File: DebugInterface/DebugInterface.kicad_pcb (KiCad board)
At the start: 2 copper layers, 157 x 169.9 mm, 38 parts, among them J1 IDC-50M, J10 Barrel_Jack_MountingPin, J11 ISP, J2 IDC-50M, J3 IDC-50M, J4 IDC-50M, J5 IDC-50M, J6 IDC-50M, J7 IDC-50M, J8 IDC-50M, J9 USB_B, U1 8255, U10 PIC18F2550-ISO, U2 8255, U3 8255, U4 8255, U5 8255, U6 8255, U7 8255, U8 8255, U9 74LS138, Y1 20MHz

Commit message: DebugInterface: Some layout touchups
Better copper fill
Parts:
- moved C8 1.50 mm to (148.8, 84.1)
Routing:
- net GND: track 1661.3 -> 1660.5 mm

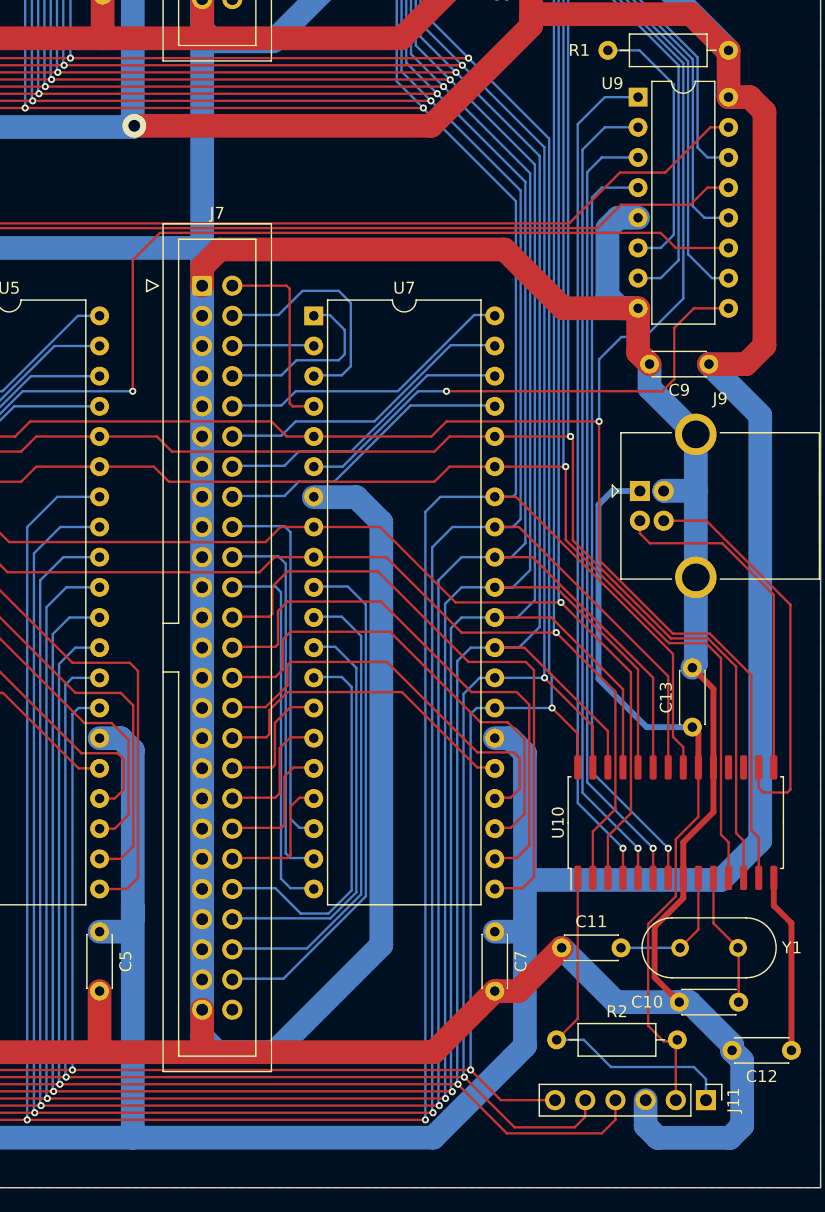
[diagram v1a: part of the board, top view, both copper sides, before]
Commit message: DebugInterface: Fix ISP connector
Proper pin assignment
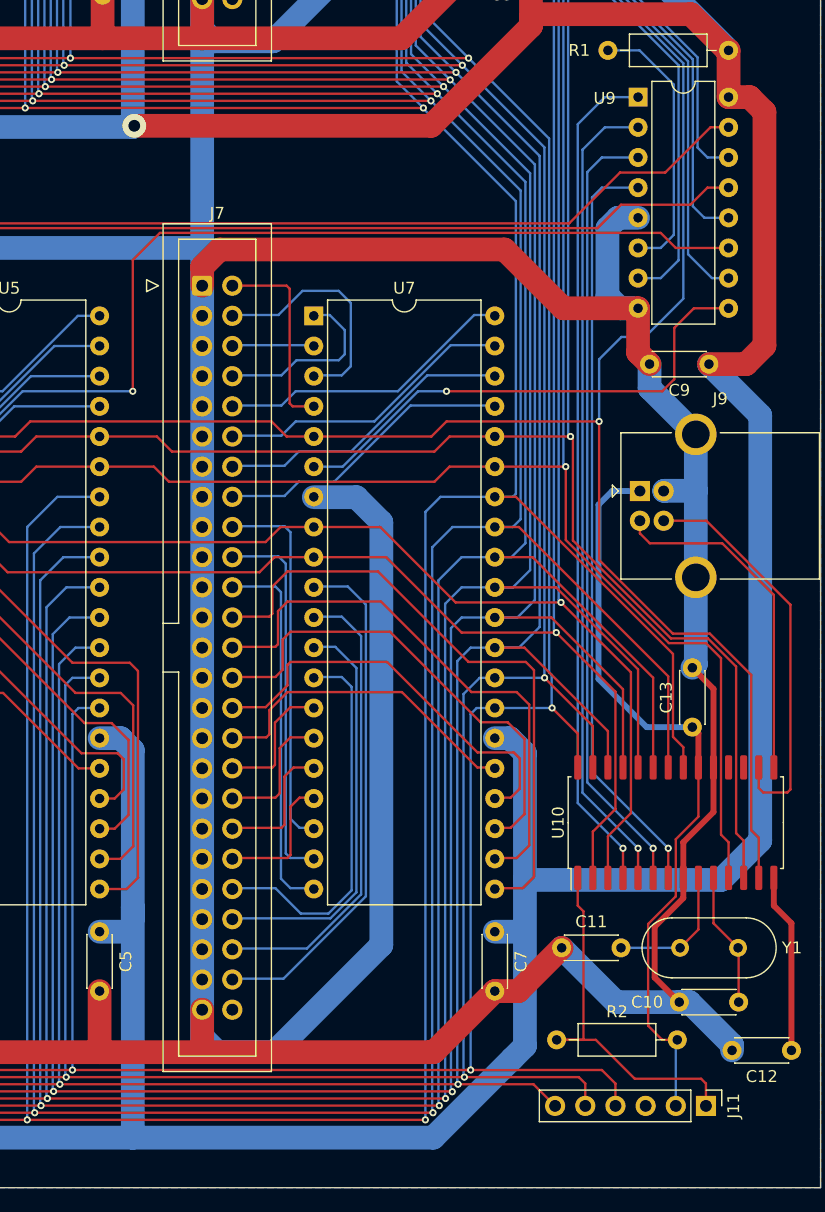
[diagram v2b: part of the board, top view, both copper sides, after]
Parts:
- moved J11 0.48 mm to (163.6, 179.8)
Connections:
- J11 pad 4: /D5 -> /D7
- J11 pad 6: /D7 -> /D5
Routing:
- net GND: track 1660.5 -> 1642.7 mm
- net /D5: track 600.2 -> 592.1 mm
- net /D7: track 535.6 -> 542.4 mm
- net Net-(J11-Pin_1): track 30.1 -> 32.1 mm
- net /D6: track 566.9 -> 565.5 mm

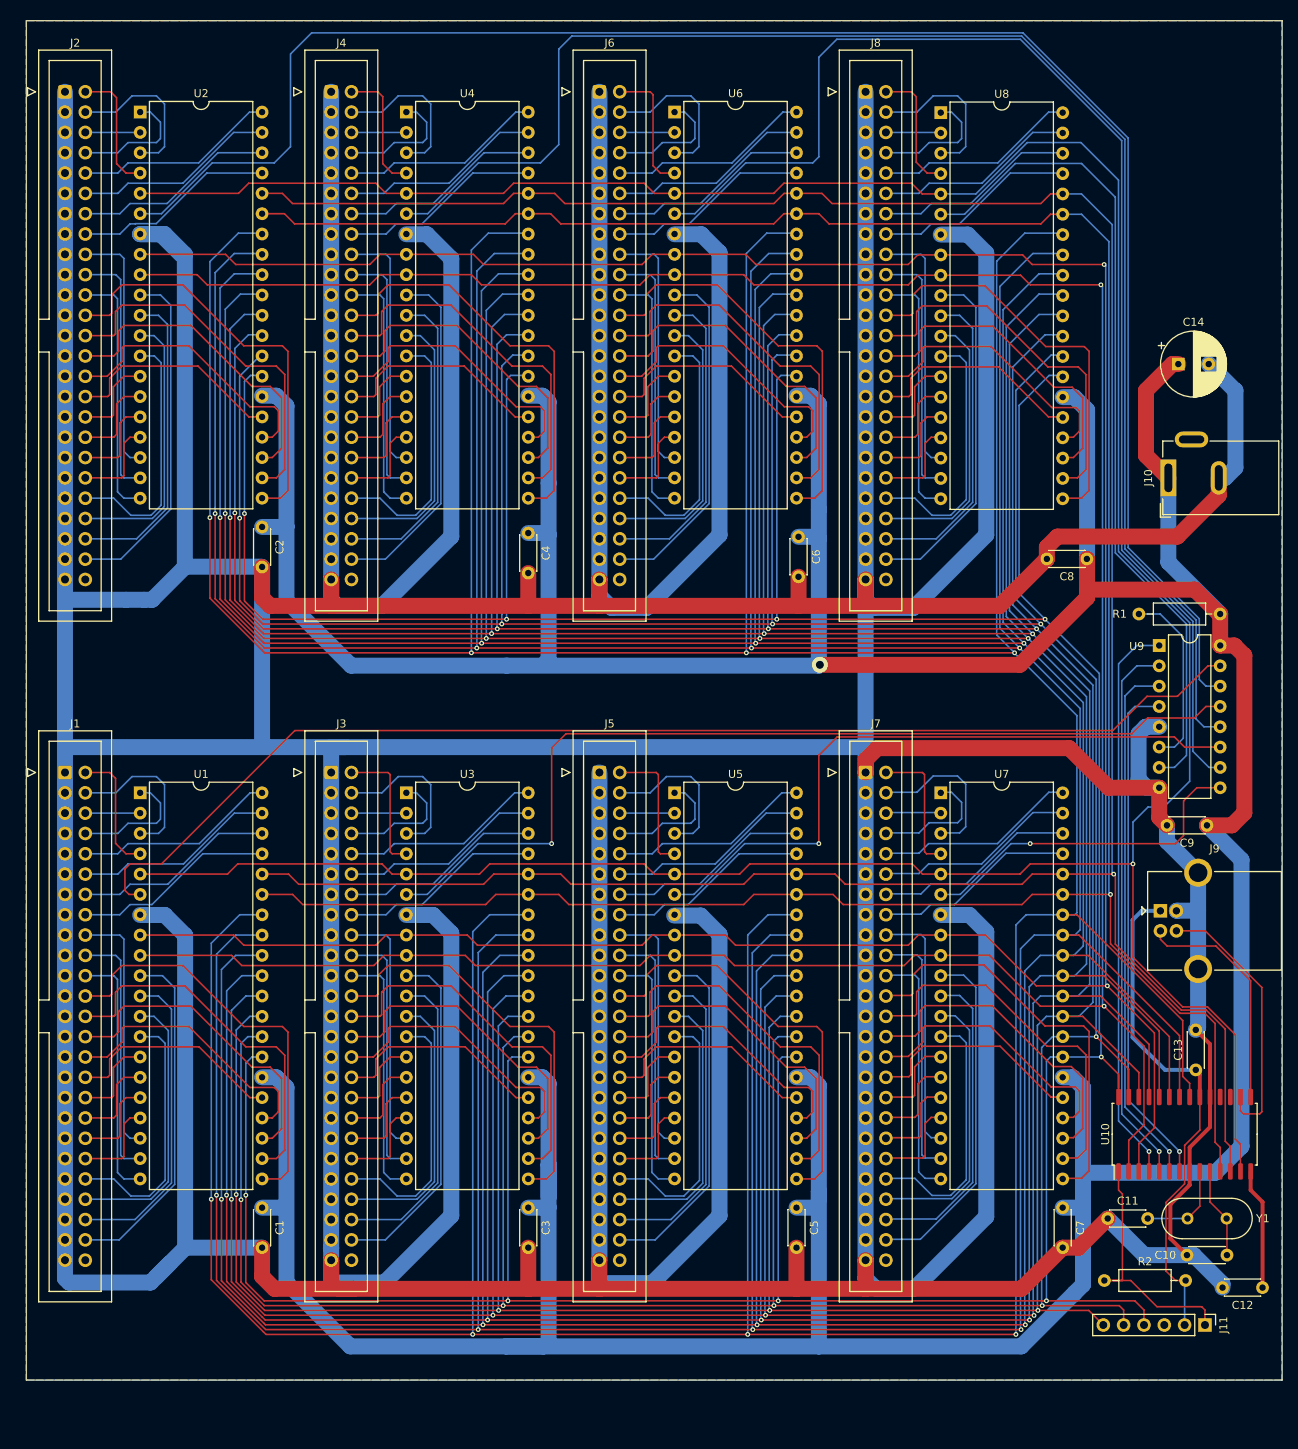
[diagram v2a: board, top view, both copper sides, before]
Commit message: DebugInterface: Second version
Each port has got own connector for ease of separation and making cables.
Ports are rearranged in address space to enable longer sequential
reads/writes
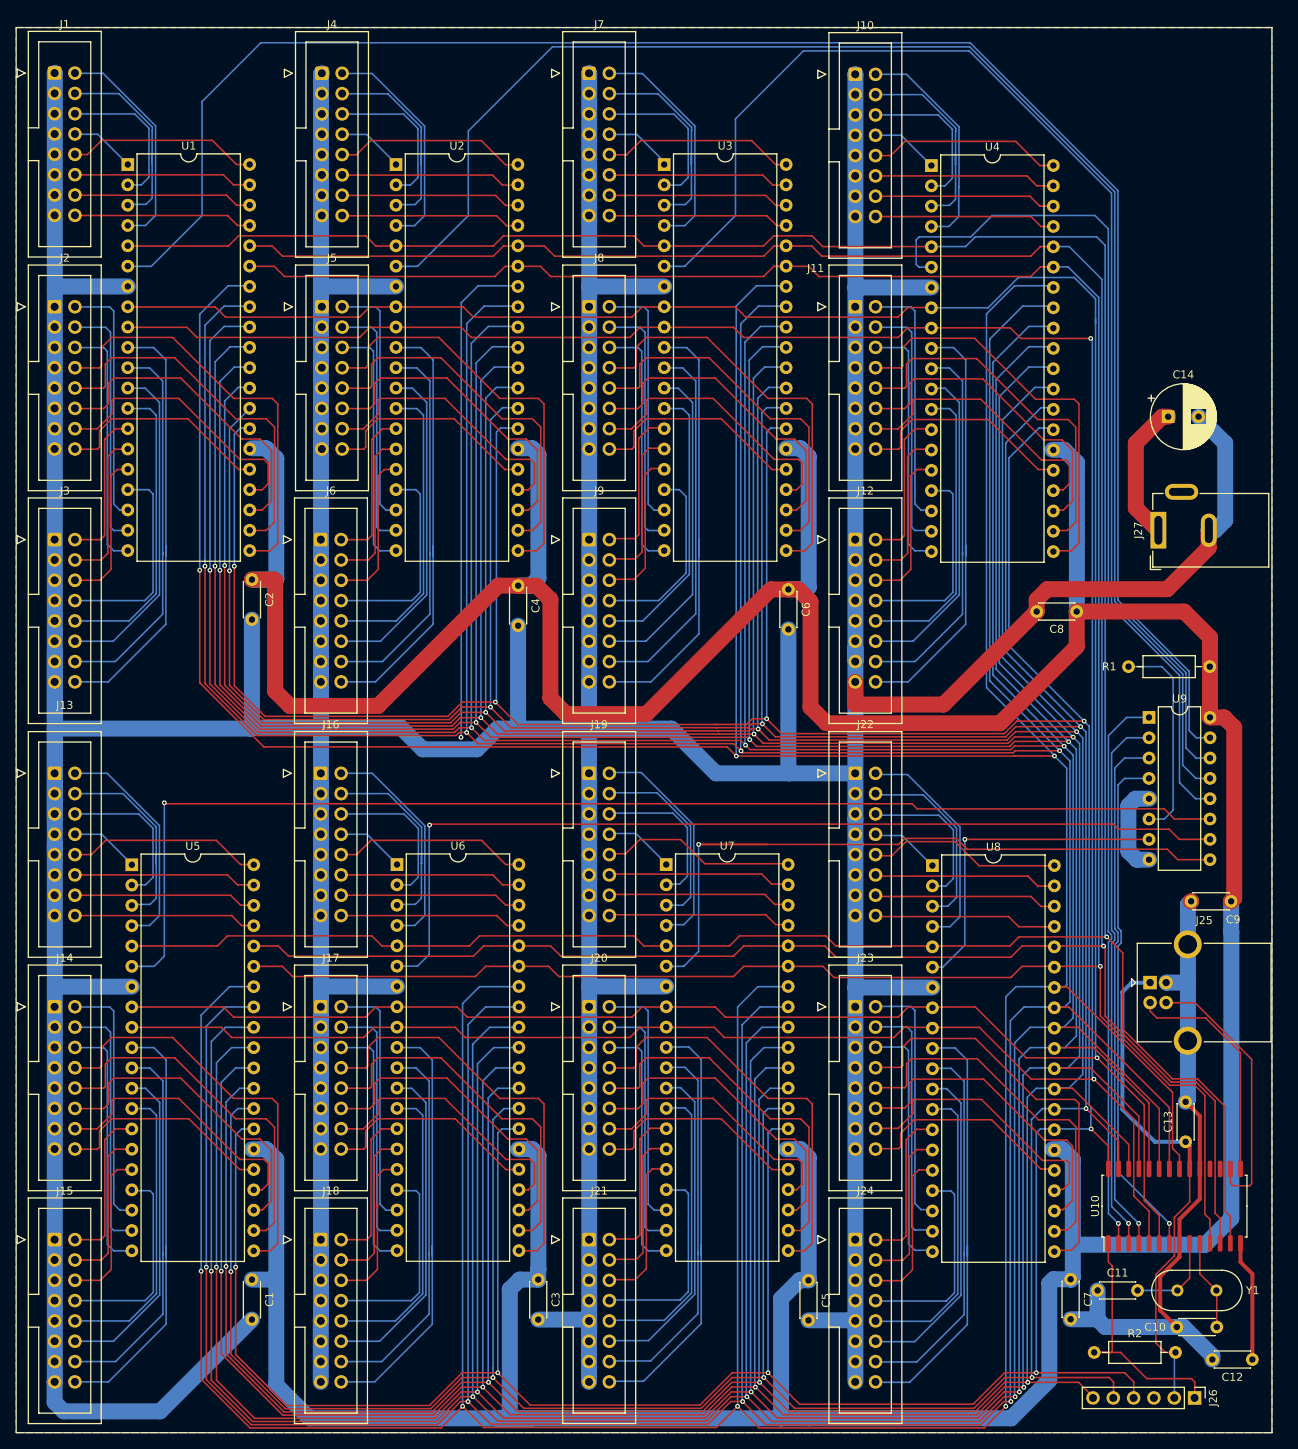
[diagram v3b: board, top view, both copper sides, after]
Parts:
- added J12: IDC-16M, Connector_IDC:IDC-Header_2x08_P2.54mm_Vertical, F.Cu at (119.9, 81.7)
- added J13: IDC-16M, Connector_IDC:IDC-Header_2x08_P2.54mm_Vertical, F.Cu at (19.8, 110.9)
- added J14: IDC-16M, Connector_IDC:IDC-Header_2x08_P2.54mm_Vertical, F.Cu at (19.8, 140.1)
- added J15: IDC-16M, Connector_IDC:IDC-Header_2x08_P2.54mm_Vertical, F.Cu at (19.8, 169.2)
- added J16: IDC-16M, Connector_IDC:IDC-Header_2x08_P2.54mm_Vertical, F.Cu at (53.1, 110.9)
- added J17: IDC-16M, Connector_IDC:IDC-Header_2x08_P2.54mm_Vertical, F.Cu at (53.1, 140.1)
- added J18: IDC-16M, Connector_IDC:IDC-Header_2x08_P2.54mm_Vertical, F.Cu at (53.1, 169.2)
- added J19: IDC-16M, Connector_IDC:IDC-Header_2x08_P2.54mm_Vertical, F.Cu at (86.6, 110.9)
- added J20: IDC-16M, Connector_IDC:IDC-Header_2x08_P2.54mm_Vertical, F.Cu at (86.6, 140.1)
- added J21: IDC-16M, Connector_IDC:IDC-Header_2x08_P2.54mm_Vertical, F.Cu at (86.6, 169.2)
- added J22: IDC-16M, Connector_IDC:IDC-Header_2x08_P2.54mm_Vertical, F.Cu at (119.9, 110.9)
- added J23: IDC-16M, Connector_IDC:IDC-Header_2x08_P2.54mm_Vertical, F.Cu at (119.9, 140.1)
- added J24: IDC-16M, Connector_IDC:IDC-Header_2x08_P2.54mm_Vertical, F.Cu at (119.9, 169.2)
- added J25: USB_B, Connector_USB:USB_B_OST_USB-B1HSxx_Horizontal, F.Cu at (156.7, 137.0)
- added J26: ISP, Connector_PinHeader_2.54mm:PinHeader_1x06_P2.54mm_Vertical, F.Cu at (162.3, 188.9)
- added J27: Barrel_Jack_MountingPin, Connector_BarrelJack:BarrelJack_GCT_DCJ200-10-A_Horizontal, F.Cu at (157.8, 80.5)
- J1, J2, J3, J4, J5, J6, J7, J8: value IDC-50M -> IDC-16M; footprint Connector_IDC:IDC-Header_2x25_P2.54mm_Vertical -> Connector_IDC:IDC-Header_2x08_P2.54mm_Vertical
- J10: value Barrel_Jack_MountingPin -> IDC-16M; footprint Connector_BarrelJack:BarrelJack_GCT_DCJ200-10-A_Horizontal -> Connector_IDC:IDC-Header_2x08_P2.54mm_Vertical
- J11: value ISP -> IDC-16M; footprint Connector_PinHeader_2.54mm:PinHeader_1x06_P2.54mm_Vertical -> Connector_IDC:IDC-Header_2x08_P2.54mm_Vertical
- J9: value USB_B -> IDC-16M; footprint Connector_USB:USB_B_OST_USB-B1HSxx_Horizontal -> Connector_IDC:IDC-Header_2x08_P2.54mm_Vertical
- moved J11 134.6 mm to (119.9, 52.6), turned to 0 degrees
- moved U6 100.3 mm to (62.6, 122.3)
- moved U8 94.1 mm to (129.5, 122.4)
- moved J7 94.0 mm to (86.6, 23.4)
- moved J1 87.4 mm to (19.8, 23.3)
- moved J9 85.2 mm to (86.6, 81.7)
- moved U3 84.9 mm to (96.0, 34.8)
- moved U1 78.6 mm to (29.0, 34.8)
- moved U5 68.4 mm to (29.5, 122.3)
- moved J5 67.8 mm to (53.2, 52.6)
- moved U4 66.0 mm to (129.4, 34.9)
- moved J6 65.9 mm to (53.1, 81.7)
- moved J10 63.8 mm to (119.9, 23.5), turned to 0 degrees
- moved J3 45.2 mm to (19.8, 81.7)
- moved J8 43.8 mm to (86.6, 52.6)
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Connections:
- C13 pad 1: Net-(J11-Pin_2) -> Net-(J25-VBUS)
- J10 pad 1: VCC -> GND
- J10 pad 2: GND -> Net-(J10-Pin_2)
- J10 pad 3: (no net) -> GND
- J11 pad 1: Net-(J11-Pin_1) -> GND
- J11 pad 4: /D7 -> Net-(J11-Pin_4)
- J11 pad 5: /D6 -> GND
- J11 pad 6: /D5 -> Net-(J11-Pin_6)
- J9 pad 1: Net-(J11-Pin_2) -> GND
- J9 pad 2: Net-(J9-D-) -> Net-(J9-Pin_2)
- J9 pad 3: Net-(J9-D+) -> GND
- J9 pad 4: GND -> Net-(J9-Pin_4)
- R2 pad 1: Net-(J11-Pin_1) -> Net-(J26-Pin_1)
- R2 pad 2: Net-(J11-Pin_2) -> Net-(J25-VBUS)
- U1 pad 10: Net-(J1-Pin_48) -> Net-(J3-Pin_16)
- U1 pad 11: Net-(J1-Pin_46) -> Net-(J3-Pin_14)
- U1 pad 12: Net-(J1-Pin_44) -> Net-(J3-Pin_12)
- U1 pad 13: Net-(J1-Pin_42) -> Net-(J3-Pin_10)
- U1 pad 14: Net-(J1-Pin_34) -> Net-(J3-Pin_2)
- U1 pad 15: Net-(J1-Pin_36) -> Net-(J3-Pin_4)
- U1 pad 16: Net-(J1-Pin_38) -> Net-(J3-Pin_6)
- U1 pad 17: Net-(J1-Pin_40) -> Net-(J3-Pin_8)
- U1 pad 18: Net-(J1-Pin_18) -> Net-(J2-Pin_2)
- U1 pad 19: Net-(J1-Pin_20) -> Net-(J2-Pin_4)
- U1 pad 20: Net-(J1-Pin_22) -> Net-(J2-Pin_6)
- U1 pad 21: Net-(J1-Pin_24) -> Net-(J2-Pin_8)
- U1 pad 22: Net-(J1-Pin_26) -> Net-(J2-Pin_10)
- U1 pad 23: Net-(J1-Pin_28) -> Net-(J2-Pin_12)
- U1 pad 24: Net-(J1-Pin_30) -> Net-(J2-Pin_14)
- U1 pad 25: Net-(J1-Pin_32) -> Net-(J2-Pin_16)
- U1 pad 8: /A1 -> /A4
- U1 pad 9: /A0 -> /A3
- U10 pad 1: Net-(J11-Pin_1) -> Net-(J26-Pin_1)
- U10 pad 15: Net-(J9-D-) -> Net-(J25-D-)
- U10 pad 16: Net-(J9-D+) -> Net-(J25-D+)
- U10 pad 20: Net-(J11-Pin_2) -> Net-(J25-VBUS)
- U2 pad 1: Net-(J2-Pin_8) -> Net-(J4-Pin_8)
- U2 pad 10: Net-(J2-Pin_48) -> Net-(J6-Pin_16)
- U2 pad 11: Net-(J2-Pin_46) -> Net-(J6-Pin_14)
- U2 pad 12: Net-(J2-Pin_44) -> Net-(J6-Pin_12)
- U2 pad 13: Net-(J2-Pin_42) -> Net-(J6-Pin_10)
- U2 pad 14: Net-(J2-Pin_34) -> Net-(J6-Pin_2)
- U2 pad 15: Net-(J2-Pin_36) -> Net-(J6-Pin_4)
- U2 pad 16: Net-(J2-Pin_38) -> Net-(J6-Pin_6)
- U2 pad 17: Net-(J2-Pin_40) -> Net-(J6-Pin_8)
- U2 pad 18: Net-(J2-Pin_18) -> Net-(J5-Pin_2)
- U2 pad 19: Net-(J2-Pin_20) -> Net-(J5-Pin_4)
- U2 pad 2: Net-(J2-Pin_6) -> Net-(J4-Pin_6)
- U2 pad 20: Net-(J2-Pin_22) -> Net-(J5-Pin_6)
- U2 pad 21: Net-(J2-Pin_24) -> Net-(J5-Pin_8)
- U2 pad 22: Net-(J2-Pin_26) -> Net-(J5-Pin_10)
- U2 pad 23: Net-(J2-Pin_28) -> Net-(J5-Pin_12)
- U2 pad 24: Net-(J2-Pin_30) -> Net-(J5-Pin_14)
- U2 pad 25: Net-(J2-Pin_32) -> Net-(J5-Pin_16)
- U2 pad 3: Net-(J2-Pin_4) -> Net-(J4-Pin_4)
- U2 pad 37: Net-(J2-Pin_16) -> Net-(J4-Pin_16)
- U2 pad 38: Net-(J2-Pin_14) -> Net-(J4-Pin_14)
- U2 pad 39: Net-(J2-Pin_12) -> Net-(J4-Pin_12)
- U2 pad 4: Net-(J2-Pin_2) -> Net-(J4-Pin_2)
- U2 pad 40: Net-(J2-Pin_10) -> Net-(J4-Pin_10)
- U2 pad 8: /A1 -> /A4
- U2 pad 9: /A0 -> /A3
- U3 pad 1: Net-(J3-Pin_8) -> Net-(J7-Pin_8)
- U3 pad 10: Net-(J3-Pin_48) -> Net-(J9-Pin_16)
- U3 pad 11: Net-(J3-Pin_46) -> Net-(J9-Pin_14)
- U3 pad 12: Net-(J3-Pin_44) -> Net-(J9-Pin_12)
- U3 pad 13: Net-(J3-Pin_42) -> Net-(J9-Pin_10)
- U3 pad 14: Net-(J3-Pin_34) -> Net-(J9-Pin_2)
- U3 pad 15: Net-(J3-Pin_36) -> Net-(J9-Pin_4)
- U3 pad 16: Net-(J3-Pin_38) -> Net-(J9-Pin_6)
- U3 pad 17: Net-(J3-Pin_40) -> Net-(J9-Pin_8)
- U3 pad 18: Net-(J3-Pin_18) -> Net-(J8-Pin_2)
- U3 pad 19: Net-(J3-Pin_20) -> Net-(J8-Pin_4)
- U3 pad 2: Net-(J3-Pin_6) -> Net-(J7-Pin_6)
- U3 pad 20: Net-(J3-Pin_22) -> Net-(J8-Pin_6)
- U3 pad 21: Net-(J3-Pin_24) -> Net-(J8-Pin_8)
- U3 pad 22: Net-(J3-Pin_26) -> Net-(J8-Pin_10)
- U3 pad 23: Net-(J3-Pin_28) -> Net-(J8-Pin_12)
- U3 pad 24: Net-(J3-Pin_30) -> Net-(J8-Pin_14)
- U3 pad 25: Net-(J3-Pin_32) -> Net-(J8-Pin_16)
- U3 pad 3: Net-(J3-Pin_4) -> Net-(J7-Pin_4)
- U3 pad 37: Net-(J3-Pin_16) -> Net-(J7-Pin_16)
- U3 pad 38: Net-(J3-Pin_14) -> Net-(J7-Pin_14)
- U3 pad 39: Net-(J3-Pin_12) -> Net-(J7-Pin_12)
- U3 pad 4: Net-(J3-Pin_2) -> Net-(J7-Pin_2)
- U3 pad 40: Net-(J3-Pin_10) -> Net-(J7-Pin_10)
- U3 pad 8: /A1 -> /A4
- U3 pad 9: /A0 -> /A3
- U4 pad 1: Net-(J4-Pin_8) -> Net-(J10-Pin_8)
- U4 pad 10: Net-(J4-Pin_48) -> Net-(J12-Pin_16)
- U4 pad 11: Net-(J4-Pin_46) -> Net-(J12-Pin_14)
- U4 pad 12: Net-(J4-Pin_44) -> Net-(J12-Pin_12)
- U4 pad 13: Net-(J4-Pin_42) -> Net-(J12-Pin_10)
- U4 pad 14: Net-(J4-Pin_34) -> Net-(J12-Pin_2)
- U4 pad 15: Net-(J4-Pin_36) -> Net-(J12-Pin_4)
- U4 pad 16: Net-(J4-Pin_38) -> Net-(J12-Pin_6)
- U4 pad 17: Net-(J4-Pin_40) -> Net-(J12-Pin_8)
- U4 pad 18: Net-(J4-Pin_18) -> Net-(J11-Pin_2)
- U4 pad 19: Net-(J4-Pin_20) -> Net-(J11-Pin_4)
- U4 pad 2: Net-(J4-Pin_6) -> Net-(J10-Pin_6)
- U4 pad 20: Net-(J4-Pin_22) -> Net-(J11-Pin_6)
- U4 pad 21: Net-(J4-Pin_24) -> Net-(J11-Pin_8)
- U4 pad 22: Net-(J4-Pin_26) -> Net-(J11-Pin_10)
- U4 pad 23: Net-(J4-Pin_28) -> Net-(J11-Pin_12)
- U4 pad 24: Net-(J4-Pin_30) -> Net-(J11-Pin_14)
- U4 pad 25: Net-(J4-Pin_32) -> Net-(J11-Pin_16)
- U4 pad 3: Net-(J4-Pin_4) -> Net-(J10-Pin_4)
- U4 pad 37: Net-(J4-Pin_16) -> Net-(J10-Pin_16)
- U4 pad 38: Net-(J4-Pin_14) -> Net-(J10-Pin_14)
- U4 pad 39: Net-(J4-Pin_12) -> Net-(J10-Pin_12)
- U4 pad 4: Net-(J4-Pin_2) -> Net-(J10-Pin_2)
- U4 pad 40: Net-(J4-Pin_10) -> Net-(J10-Pin_10)
- U4 pad 8: /A1 -> /A4
- U4 pad 9: /A0 -> /A3
- U5 pad 1: Net-(J5-Pin_8) -> Net-(J13-Pin_8)
- U5 pad 10: Net-(J5-Pin_48) -> Net-(J15-Pin_16)
- U5 pad 11: Net-(J5-Pin_46) -> Net-(J15-Pin_14)
- U5 pad 12: Net-(J5-Pin_44) -> Net-(J15-Pin_12)
- U5 pad 13: Net-(J5-Pin_42) -> Net-(J15-Pin_10)
- U5 pad 14: Net-(J5-Pin_34) -> Net-(J15-Pin_2)
- U5 pad 15: Net-(J5-Pin_36) -> Net-(J15-Pin_4)
- U5 pad 16: Net-(J5-Pin_38) -> Net-(J15-Pin_6)
- U5 pad 17: Net-(J5-Pin_40) -> Net-(J15-Pin_8)
- U5 pad 18: Net-(J5-Pin_18) -> Net-(J14-Pin_2)
- U5 pad 19: Net-(J5-Pin_20) -> Net-(J14-Pin_4)
- U5 pad 2: Net-(J5-Pin_6) -> Net-(J13-Pin_6)
- U5 pad 20: Net-(J5-Pin_22) -> Net-(J14-Pin_6)
- U5 pad 21: Net-(J5-Pin_24) -> Net-(J14-Pin_8)
- U5 pad 22: Net-(J5-Pin_26) -> Net-(J14-Pin_10)
- U5 pad 23: Net-(J5-Pin_28) -> Net-(J14-Pin_12)
- U5 pad 24: Net-(J5-Pin_30) -> Net-(J14-Pin_14)
- U5 pad 25: Net-(J5-Pin_32) -> Net-(J14-Pin_16)
- U5 pad 3: Net-(J5-Pin_4) -> Net-(J13-Pin_4)
- U5 pad 37: Net-(J5-Pin_16) -> Net-(J13-Pin_16)
- U5 pad 38: Net-(J5-Pin_14) -> Net-(J13-Pin_14)
- U5 pad 39: Net-(J5-Pin_12) -> Net-(J13-Pin_12)
- U5 pad 4: Net-(J5-Pin_2) -> Net-(J13-Pin_2)
- U5 pad 40: Net-(J5-Pin_10) -> Net-(J13-Pin_10)
- U5 pad 8: /A1 -> /A4
- U5 pad 9: /A0 -> /A3
- U6 pad 1: Net-(J6-Pin_8) -> Net-(J16-Pin_8)
- U6 pad 10: Net-(J6-Pin_48) -> Net-(J18-Pin_16)
- U6 pad 11: Net-(J6-Pin_46) -> Net-(J18-Pin_14)
- U6 pad 12: Net-(J6-Pin_44) -> Net-(J18-Pin_12)
- U6 pad 13: Net-(J6-Pin_42) -> Net-(J18-Pin_10)
- U6 pad 14: Net-(J6-Pin_34) -> Net-(J18-Pin_2)
- U6 pad 15: Net-(J6-Pin_36) -> Net-(J18-Pin_4)
- U6 pad 16: Net-(J6-Pin_38) -> Net-(J18-Pin_6)
- U6 pad 17: Net-(J6-Pin_40) -> Net-(J18-Pin_8)
- U6 pad 18: Net-(J6-Pin_18) -> Net-(J17-Pin_2)
- U6 pad 19: Net-(J6-Pin_20) -> Net-(J17-Pin_4)
- U6 pad 2: Net-(J6-Pin_6) -> Net-(J16-Pin_6)
- U6 pad 20: Net-(J6-Pin_22) -> Net-(J17-Pin_6)
- U6 pad 21: Net-(J6-Pin_24) -> Net-(J17-Pin_8)
- U6 pad 22: Net-(J6-Pin_26) -> Net-(J17-Pin_10)
- U6 pad 23: Net-(J6-Pin_28) -> Net-(J17-Pin_12)
- U6 pad 24: Net-(J6-Pin_30) -> Net-(J17-Pin_14)
- U6 pad 25: Net-(J6-Pin_32) -> Net-(J17-Pin_16)
- U6 pad 3: Net-(J6-Pin_4) -> Net-(J16-Pin_4)
- U6 pad 37: Net-(J6-Pin_16) -> Net-(J16-Pin_16)
- U6 pad 38: Net-(J6-Pin_14) -> Net-(J16-Pin_14)
- U6 pad 39: Net-(J6-Pin_12) -> Net-(J16-Pin_12)
- U6 pad 4: Net-(J6-Pin_2) -> Net-(J16-Pin_2)
- U6 pad 40: Net-(J6-Pin_10) -> Net-(J16-Pin_10)
- U6 pad 8: /A1 -> /A4
- U6 pad 9: /A0 -> /A3
- U7 pad 1: Net-(J7-Pin_8) -> Net-(J19-Pin_8)
- U7 pad 10: Net-(J7-Pin_48) -> Net-(J21-Pin_16)
- U7 pad 11: Net-(J7-Pin_46) -> Net-(J21-Pin_14)
- U7 pad 12: Net-(J7-Pin_44) -> Net-(J21-Pin_12)
- U7 pad 13: Net-(J7-Pin_42) -> Net-(J21-Pin_10)
- U7 pad 14: Net-(J7-Pin_34) -> Net-(J21-Pin_2)
- U7 pad 15: Net-(J7-Pin_36) -> Net-(J21-Pin_4)
- U7 pad 16: Net-(J7-Pin_38) -> Net-(J21-Pin_6)
- U7 pad 17: Net-(J7-Pin_40) -> Net-(J21-Pin_8)
- U7 pad 18: Net-(J7-Pin_18) -> Net-(J20-Pin_2)
- U7 pad 19: Net-(J7-Pin_20) -> Net-(J20-Pin_4)
- U7 pad 2: Net-(J7-Pin_6) -> Net-(J19-Pin_6)
- U7 pad 20: Net-(J7-Pin_22) -> Net-(J20-Pin_6)
- U7 pad 21: Net-(J7-Pin_24) -> Net-(J20-Pin_8)
- U7 pad 22: Net-(J7-Pin_26) -> Net-(J20-Pin_10)
- U7 pad 23: Net-(J7-Pin_28) -> Net-(J20-Pin_12)
- U7 pad 24: Net-(J7-Pin_30) -> Net-(J20-Pin_14)
- U7 pad 25: Net-(J7-Pin_32) -> Net-(J20-Pin_16)
- U7 pad 3: Net-(J7-Pin_4) -> Net-(J19-Pin_4)
- U7 pad 37: Net-(J7-Pin_16) -> Net-(J19-Pin_16)
- U7 pad 38: Net-(J7-Pin_14) -> Net-(J19-Pin_14)
- U7 pad 39: Net-(J7-Pin_12) -> Net-(J19-Pin_12)
- U7 pad 4: Net-(J7-Pin_2) -> Net-(J19-Pin_2)
- U7 pad 40: Net-(J7-Pin_10) -> Net-(J19-Pin_10)
- U7 pad 8: /A1 -> /A4
- U7 pad 9: /A0 -> /A3
- U8 pad 1: Net-(J8-Pin_8) -> Net-(J22-Pin_8)
- U8 pad 10: Net-(J8-Pin_48) -> Net-(J24-Pin_16)
- U8 pad 11: Net-(J8-Pin_46) -> Net-(J24-Pin_14)
- U8 pad 12: Net-(J8-Pin_44) -> Net-(J24-Pin_12)
- U8 pad 13: Net-(J8-Pin_42) -> Net-(J24-Pin_10)
- U8 pad 14: Net-(J8-Pin_34) -> Net-(J24-Pin_2)
- U8 pad 15: Net-(J8-Pin_36) -> Net-(J24-Pin_4)
- U8 pad 16: Net-(J8-Pin_38) -> Net-(J24-Pin_6)
- U8 pad 17: Net-(J8-Pin_40) -> Net-(J24-Pin_8)
- U8 pad 18: Net-(J8-Pin_18) -> Net-(J23-Pin_2)
- U8 pad 19: Net-(J8-Pin_20) -> Net-(J23-Pin_4)
- U8 pad 2: Net-(J8-Pin_6) -> Net-(J22-Pin_6)
- U8 pad 20: Net-(J8-Pin_22) -> Net-(J23-Pin_6)
- U8 pad 21: Net-(J8-Pin_24) -> Net-(J23-Pin_8)
- U8 pad 22: Net-(J8-Pin_26) -> Net-(J23-Pin_10)
- U8 pad 23: Net-(J8-Pin_28) -> Net-(J23-Pin_12)
- U8 pad 24: Net-(J8-Pin_30) -> Net-(J23-Pin_14)
- U8 pad 25: Net-(J8-Pin_32) -> Net-(J23-Pin_16)
- U8 pad 3: Net-(J8-Pin_4) -> Net-(J22-Pin_4)
- U8 pad 37: Net-(J8-Pin_16) -> Net-(J22-Pin_16)
- U8 pad 38: Net-(J8-Pin_14) -> Net-(J22-Pin_14)
- U8 pad 39: Net-(J8-Pin_12) -> Net-(J22-Pin_12)
- U8 pad 4: Net-(J8-Pin_2) -> Net-(J22-Pin_2)
- U8 pad 40: Net-(J8-Pin_10) -> Net-(J22-Pin_10)
- U8 pad 8: /A1 -> /A4
- U8 pad 9: /A0 -> /A3
- U9 pad 1: /A2 -> /A0
- U9 pad 2: /A3 -> /A1
- U9 pad 3: /A4 -> /A2
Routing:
- net GND: track 1642.7 -> 1124.7 mm
- net /A4: track 66.5 -> 375.0 mm
- net /A1: track 367.6 -> 68.0 mm, vias 2 -> 1
- net /A3: track 68.7 -> 366.3 mm, vias 1 -> 2
- net /A0: track 363.8 -> 70.4 mm, vias 2 -> 1
- net /~{CS3}: track 190.9 -> 108.6 mm
- net /~{CS0}: track 152.2 -> 225.3 mm
- net /~{CS4}: track 83.4 -> 155.3 mm
- net Net-(J25-VBUS): track 0.00 -> 63.7 mm
- net /~{CS7}: track 103.7 -> 41.4 mm, vias 0 -> 1
- net Net-(J9-Pin_16): track 0.00 -> 55.0 mm
- net Net-(J21-Pin_16): track 0.00 -> 53.6 mm
- net Net-(J24-Pin_16): track 0.00 -> 53.6 mm
- net Net-(J18-Pin_16): track 0.00 -> 53.6 mm
- net Net-(J15-Pin_16): track 0.00 -> 53.6 mm
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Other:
- board size 157 x 169.9 mm -> 157 x 175.6 mm
